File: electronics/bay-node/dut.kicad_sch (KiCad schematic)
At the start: 24 parts, among them J5 AUX, Q2 2N7002, Q3 2N7002, U10 INA226AIDGSR, U9 TPS2553DBVR

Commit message: Hub 37 and node 38 part types: more values merged
From the JLC cost session's list (it does the analysis, this session
edits the boards).  No footprint or track moves; both boards regenerated
on their Freerouting sessions (node 996/386, hub 1241/593 segments/vias),
ERC 0, DRC 0 errors (the hub's known C8 silkscreen warning), parity 0.

- Hub: the IMON filters and the CAN split caps on the dVdT caps' 22 nF
  (IMON RC 22 µs; the split cap only filters common mode): 38 -> 37 types,
  -$17.05 of feeders against the quote, order ≈ $212.77.
- Node: buck EN 100k/10k (same 13.5 V / 10.8 V), PC_DET 10k/18k (3.2 V),
  I²C pull-ups 5.1k, AUX VREF 33 Ω: 42 -> 38 types, estimate ≈ $322.77.

Docs: electronics.md (the hub's types per block, the node's estimate),
can.md, firmware pin tables.

Co-Authored-By: Claude Opus 5.5 <noreply@anthropic.com>
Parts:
- R21, R22: value 4.7k -> 5.1k; LCSC C23162 -> C23186; MPN 0603WAF4701T5E -> 0603WAF5101T5E
- R23: value 10 -> 33; LCSC C22859 -> C23140; MPN 0603WAF100JT5E -> 0603WAF330JT5E
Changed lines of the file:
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@@
 			)
 		)
-		(property "Value" "4.7k"
+		(property "Value" "5.1k"
 			(at 258.116 53.34 0)
 			(effects
@@
 			)
 		)
-		(property "Description" "Resistor 4.7k 0603"
+		(property "Description" "Resistor 5.1k 0603"
 			(at 254 52.07 0)
 			(effects
@@
 			)
 		)
-		(property "LCSC" "C23162"
+		(property "LCSC" "C23186"
 			(at 254 52.07 0)
 			(effects
@@
 			)
 		)
-		(property "MPN" "0603WAF4701T5E"
+		(property "MPN" "0603WAF5101T5E"
 			(at 254 52.07 0)
 			(effects
@@
 			)
 		)
-		(property "Value" "4.7k"
+		(property "Value" "5.1k"
 			(at 278.436 53.34 0)
 			(effects
@@
 			)
 		)
-		(property "Description" "Resistor 4.7k 0603"
+		(property "Description" "Resistor 5.1k 0603"
 			(at 274.32 52.07 0)
 			(effects
@@
 			)
 		)
-		(property "LCSC" "C23162"
+		(property "LCSC" "C23186"
 			(at 274.32 52.07 0)
 			(effects
@@
 			)
 		)
-		(property "MPN" "0603WAF4701T5E"
+		(property "MPN" "0603WAF5101T5E"
 			(at 274.32 52.07 0)
 			(effects
@@
 			)
 		)
-		(property "Value" "10"
+		(property "Value" "33"
 			(at 229.87 139.776 90)
 			(effects
@@
 			)
 		)
-		(property "Description" "Resistor 10 0603"
+		(property "Description" "Resistor 33 0603"
 			(at 229.87 137.16 0)
 			(effects
@@
 			)
 		)
-		(property "LCSC" "C22859"
+		(property "LCSC" "C23140"
 			(at 229.87 137.16 0)
 			(effects
@@
 			)
 		)
-		(property "MPN" "0603WAF100JT5E"
+		(property "MPN" "0603WAF330JT5E"
 			(at 229.87 137.16 0)
 			(effects
@@
 		)
 	)
-	(text_box "TPS2553: ILIM 18k → 1.34–1.52 A.  EN is pulled up: DUT_5V is on\n  even with no firmware; ~FAULT flags current limit / over-temperature.\nINA226 (I2C 0x40) runs from +3V3: it measures the drop across\n  R19 (50 mΩ → 1.64 A full scale, Kelvin sense pads); Vbus on Vin-: DUT_5V at the shunt.\nAUX: TX/RX through 1k, VREF = +3V3 through 10 Ω (level hint),\n  RESET/BOOT open-drain (2N7002, 100k gate pull-downs)."
+	(text_box "TPS2553: ILIM 18k → 1.34–1.52 A.  EN is pulled up: DUT_5V is on\n  even with no firmware; ~FAULT flags current limit / over-temperature.\nINA226 (I2C 0x40) runs from +3V3: it measures the drop across\n  R19 (50 mΩ → 1.64 A full scale, Kelvin sense pads); Vbus on Vin-: DUT_5V at the shunt.\nAUX: TX/RX through 1k, VREF = +3V3 through 33 Ω (level hint),\n  RESET/BOOT open-drain (2N7002, 100k gate pull-downs)."
 		(exclude_from_sim no)
 		(at 15.24 132.08 0)

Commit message: Node U9 TPS2553D; hub input FETs stay 40 V
Three checks from a BOM review:

- Node U9: the TPS2553DDBVR (C521201, $0.19 against $0.54) instead of
  the TPS2553DBVR.  Same SOT-23-6 pinout (IN GND EN FAULT ILIM OUT, EN
  active high), the same I_LIM equations (18k: 1.34-1.52 A), 85 mΩ,
  constant current then thermal cycling, plus reverse-voltage
  protection.  JLC's EasyEDA footprint for it is turned 90° from the old
  part's: CPL correction 270° (fitted pad by pad, as the TPS2553-1's).
  There is no latch-off D part: the DATA x4 keeps the TPS2553DBVR-1.
- Hub Q1/Q2 stay IRF7842 (40 V).  The AP33772S drives the gate at most
  4 V above VCC, so R_DS(on) at 4.5 V decides (5.9 mΩ max); Diodes' EVB
  uses 30 V parts; 60 V SO-8 parts in stock are ≥ 28 mΩ there.  Q1 sees
  > 40 V only with the switch open, VRACK discharged and a > 4 A surge
  into the SMAJ30A; the IRF7842 is avalanche-rated (50 mJ, 14 A).
- Node C11 stays 0805: a 1206 overlaps U2 and its neighbours.

The node regenerated on its Freerouting session (996 segments, 386
vias): ERC 0, DRC 0, parity 0.  Estimate ≈ $318.85.

Co-Authored-By: Claude Opus 5.5 <noreply@anthropic.com>
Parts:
- U9: value TPS2553DBVR -> TPS2553DDBVR; Alternative (none) -> TPS2553DBVR (C55266, the original, same pinout and I_LIM eq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; LCSC C55266 -> C521201; MPN TPS2553DBVR -> TPS2553DDBVR
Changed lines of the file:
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@@
 			)
 		)
-		(property "Value" "TPS2553DBVR"
-			(at 97.215 68.58 0)
+		(property "Value" "TPS2553DDBVR"
+			(at 97.74 68.58 0)
 			(effects
 				(font
@@
 			)
 		)
-		(property "Datasheet" "https://www.ti.com/lit/ds/symlink/tps2553.pdf"
+		(property "Datasheet" "https://www.ti.com/lit/ds/symlink/tps2553d.pdf"
 			(at 101.6 76.2 0)
 			(effects
@@
 			)
 		)
-		(property "MPN" "TPS2553DBVR"
+		(property "MPN" "TPS2553DDBVR"
 			(at 101.6 76.2 0)
 			(effects
@@
 			)
 		)
-		(property "LCSC" "C55266"
+		(property "LCSC" "C521201"
 			(at 101.6 76.2 0)
 			(effects
+				(font
+					(size 1.27 1.27)
+				)
+				(hide yes)
+			)
+		)
+		(property "Alternative" "TPS2553DBVR (C55266, the original, same pinout and I_LIM equations)"
+			(at 101.6 76.2 0)
+			(effects

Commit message: PCBA review: hub and node fixes before the order
On main's CH224A hub and the bay node v0.5.

Power hub:
- CPL: the side LEDs (C598310, C4555382) +0.825 mm, their polarity
  proven from JLC's own footprints (and C495809 at 270 deg in the table,
  for the IRF7842 the AP33772S hub had).
- Rows: SHDN pull-downs 10k, so rows stay off without firmware (100k
  gave 1 V at the pin's 10 uA); a B5819W at each row output for the
  cable's kick; the red FAULT LEDs fed from their ROW_EN, so a row that
  is simply off shows no fault.
- In2's VRACK band 8 mm wide; the console's USB pair hand-routed on
  F.Cu over In1 (U5's channels in the pair's order), EN's capacitor at
  the module's pin; reliefs on both pads of C2, C10, R3, C11-C14; notes
  corrected, the outputs sheet on A2.
- The PESD2CAN kept and documented (no stocked CAN TVS stays off at
  29.4 V and clamps under +40 V).

Bay node:
- SW3 placed on its pegs (-0.55 mm, Shouhan's land pattern); 2.2k I2C
  pull-ups; POS_IN 470k; AUX_VREF 1k; 100k on SVC; U9's input on a +5V
  island with three vias, C20 at its pins; C12 relieved; the camera note
  and the catalog's MPN text corrected.

Both re-routed: ERC 0, DRC 0 (the known C8 silkscreen warning), parity
0; CPL audit against JLC's footprints: every part agrees but SW3's pads
(0.13 mm, on purpose).  Bring-up measurements in assembly.md, the
resolution in pcba-review.md.

Co-Authored-By: Claude Opus 5.5 <noreply@anthropic.com>
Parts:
- R19: MPN HoLR1206-1W-50mR-1% -> HoLR1206-1W-50mR-1%-75ppm
- R21, R22: value 5.1k -> 2.2k; LCSC C23186 -> C4190; MPN 0603WAF5101T5E -> 0603WAF2201T5E
- R23: value 33 -> 1k; LCSC C23140 -> C21190; MPN 0603WAF330JT5E -> 0603WAF1001T5E
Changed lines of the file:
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@@
 			)
 		)
-		(property "MPN" "HoLR1206-1W-50mR-1%"
+		(property "MPN" "HoLR1206-1W-50mR-1%-75ppm"
 			(at 157.48 85.09 0)
 			(effects
@@
 			)
 		)
-		(property "Value" "5.1k"
+		(property "Value" "2.2k"
 			(at 258.116 53.34 0)
 			(effects
@@
 			)
 		)
-		(property "Description" "Resistor 5.1k 0603"
+		(property "Description" "Resistor 2.2k 0603"
 			(at 254 52.07 0)
 			(effects
@@
 			)
 		)
-		(property "LCSC" "C23186"
+		(property "LCSC" "C4190"
 			(at 254 52.07 0)
 			(effects
@@
 			)
 		)
-		(property "MPN" "0603WAF5101T5E"
+		(property "MPN" "0603WAF2201T5E"
 			(at 254 52.07 0)
 			(effects
@@
 			)
 		)
-		(property "Value" "5.1k"
+		(property "Value" "2.2k"
 			(at 278.436 53.34 0)
 			(effects
@@
 			)
 		)
-		(property "Description" "Resistor 5.1k 0603"
+		(property "Description" "Resistor 2.2k 0603"
 			(at 274.32 52.07 0)
 			(effects
@@
 			)
 		)
-		(property "LCSC" "C23186"
+		(property "LCSC" "C4190"
 			(at 274.32 52.07 0)
 			(effects
@@
 			)
 		)
-		(property "MPN" "0603WAF5101T5E"
+		(property "MPN" "0603WAF2201T5E"
 			(at 274.32 52.07 0)
 			(effects
@@
 			)
 		)
-		(property "Value" "33"
+		(property "Value" "1k"
 			(at 229.87 139.776 90)
 			(effects
@@
 			)
 		)
-		(property "Description" "Resistor 33 0603"
+		(property "Description" "Resistor 1k 0603"
 			(at 229.87 137.16 0)
 			(effects
@@
 			)
 		)
-		(property "LCSC" "C23140"
+		(property "LCSC" "C21190"
 			(at 229.87 137.16 0)
 			(effects
@@
 			)
 		)
-		(property "MPN" "0603WAF330JT5E"
+		(property "MPN" "0603WAF1001T5E"
 			(at 229.87 137.16 0)
 			(effects

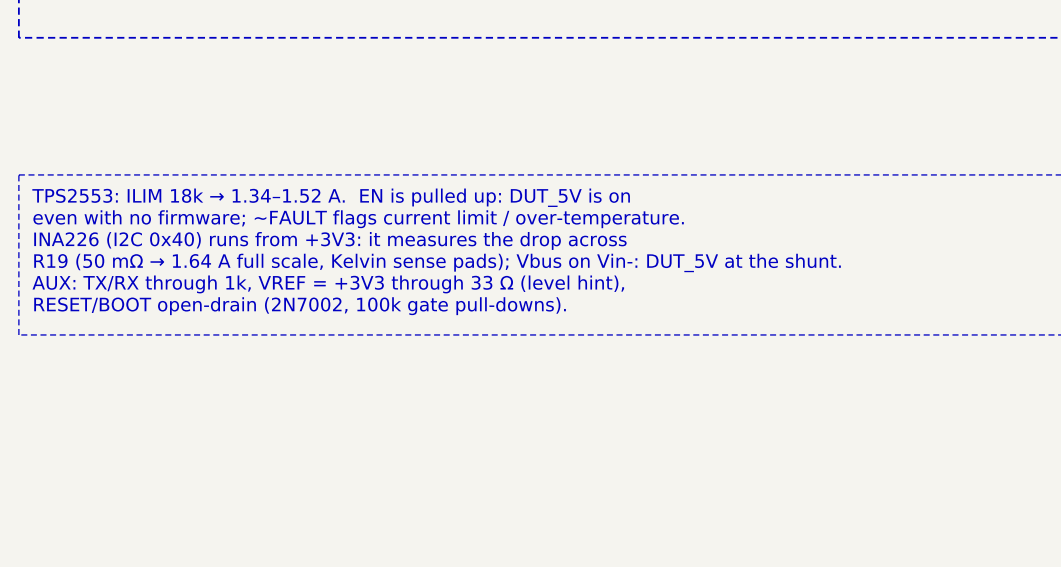
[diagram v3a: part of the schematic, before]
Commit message: Bay node: AP2114H for the 3.3 V, camera ESD clamped to +3V3
The schematic counter-review's fixes, approved by the user.

- U2: AP2114H-3.3TRG1 (C150716, catalog ldo_1a) instead of the AMS1117-3.3.
  It is specified stable with ceramics (C11, C12); the AMS1117 guarantees it
  only with 22 uF tantalum.  Same SOT-223 "H" pinout (1 GND, 2 and tab VOUT,
  3 VIN), footprint and copper: only the part's properties change.
- U12, U13 (USBLC6 on the camera lead): pin 5 on +3V3 instead of CAM_5V.
  With CAM_5V off (the PTC tripped), the SPI lines would feed the pod through
  the upper diodes, and CAM_5V's clamp sits above the ESP32's 3.6 V.  A
  minimal patch of the routing, no re-route: the CAM_5V stub that only
  reached the two pins goes (10 segments); U12.5 gets a +3V3 feed to a via in
  In2's +3V3 area; U13.5, with no room for its own, joins U12.5 along the
  stub's old east path at 0.25 mm.  The straightening pass ran on +3V3 and
  CAM_5V.
- Stale notes: AUX_VREF goes through R23's 1k, not 33 ohms; the next node's
  pull-down is R29's 470k, not 100k.
- pcbgen.fanout_pads takes `only` (REF.PAD), to fan out a few pads of a
  routed board.

ERC 0, DRC 0, unconnected 0, parity 0, every 3D model found.  The renders,
Gerbers and viewer model are regenerated (the unchanged iso render kept).
The schematic, the BOM and the docs (the node table, the CPL fix table, the
bring-up check, PCBA review N9) follow.  The hub and bom/ are untouched.

Co-Authored-By: Claude Opus 5.5 <noreply@anthropic.com>
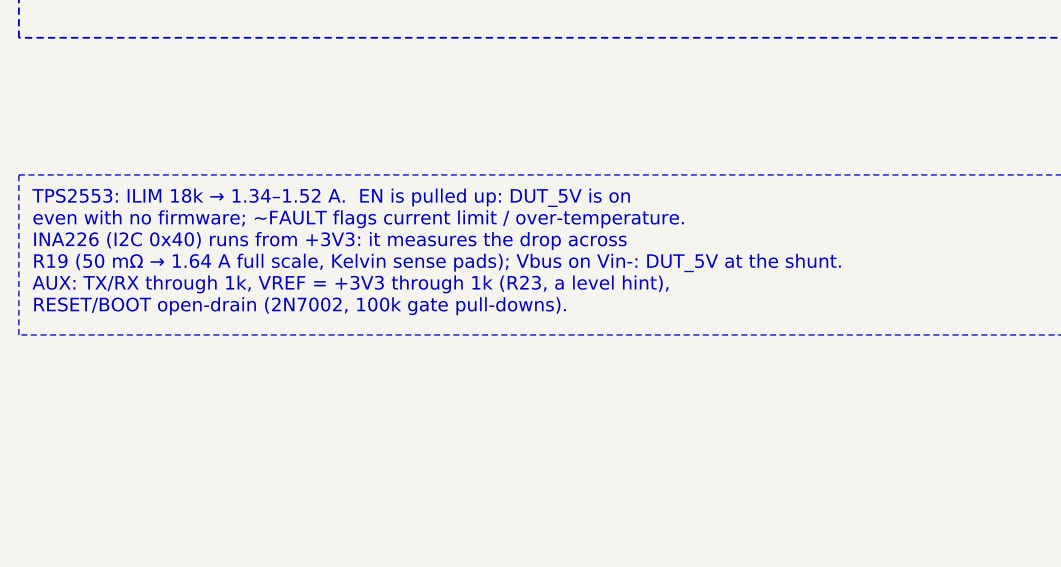
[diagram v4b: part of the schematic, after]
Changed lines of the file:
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@@
 		)
 	)
-	(text_box "TPS2553: ILIM 18k → 1.34–1.52 A.  EN is pulled up: DUT_5V is on\n  even with no firmware; ~FAULT flags current limit / over-temperature.\nINA226 (I2C 0x40) runs from +3V3: it measures the drop across\n  R19 (50 mΩ → 1.64 A full scale, Kelvin sense pads); Vbus on Vin-: DUT_5V at the shunt.\nAUX: TX/RX through 1k, VREF = +3V3 through 33 Ω (level hint),\n  RESET/BOOT open-drain (2N7002, 100k gate pull-downs)."
+	(text_box "TPS2553: ILIM 18k → 1.34–1.52 A.  EN is pulled up: DUT_5V is on\n  even with no firmware; ~FAULT flags current limit / over-temperature.\nINA226 (I2C 0x40) runs from +3V3: it measures the drop across\n  R19 (50 mΩ → 1.64 A full scale, Kelvin sense pads); Vbus on Vin-: DUT_5V at the shunt.\nAUX: TX/RX through 1k, VREF = +3V3 through 1k (R23, a level hint),\n  RESET/BOOT open-drain (2N7002, 100k gate pull-downs)."
 		(exclude_from_sim no)
 		(at 15.24 132.08 0)

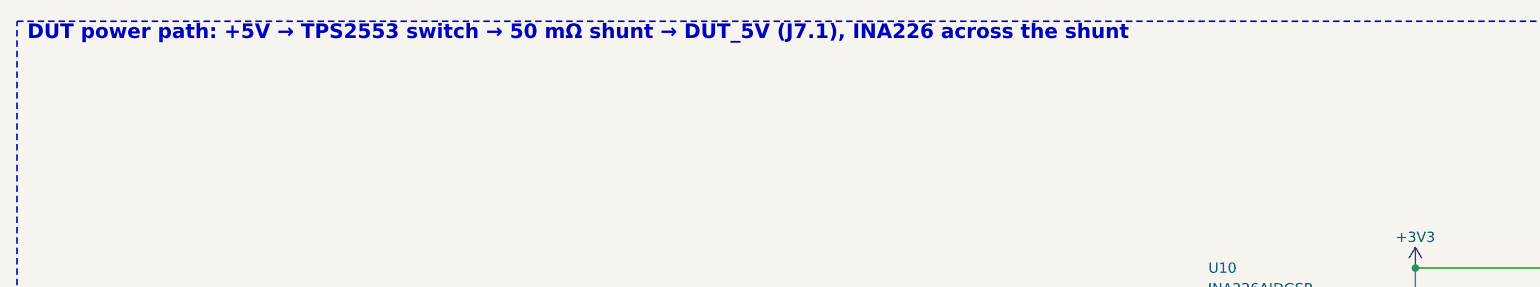
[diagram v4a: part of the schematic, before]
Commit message: Datasheet audit F1-F6: the pod's AP2114H, STB 5.1k, PC_DET hysteresis, the camera ESD's 100 nF, the eFuse step
The user approved the audit's fixes for the node, the hub and the pod
("Go pour 1"); docs/datasheet-audit.md marks F1-F6 applied.

* F1, camera pod: U1 AMS1117-3.3 -> AP2114H-3.3TRG1 (C150716, catalog
  ldo_1a, the node's U2).
  - The AMS1117 is specified stable only with 22 uF tantalum; the
    AP2114H is stable with the ceramic C2.
  - Same SOT-223 pinout, copper (the +3V3 pour and island round the
    tab stay) and 180 deg CPL correction.
  - One more extended type on the pod's Economic order: +$3.09 and
    $0.05 of parts (JLC_SINCE_QUOTE).
* F2, power hub: R214 (TJA1462 STB pull-down) 10k -> 5.1k (C23186,
  already on the board). With IO9 floating, STB's internal pull-up
  (20 kOhm minimum) left it at up to 1.10 V, over VIL 0.99 V.
* F3, bay node: R42 150k from MUX_SEL back to PC_DET, beside U7 (C22807,
  on the board since S1).
  - The laptop's VBUS rises at ~50 us/V through R11/R12, where the
    LVC1G32 wants <= 10 ns/V and warns of oscillation.
  - This gives ~0.14 V of hysteresis.
* F4, bay node: C28 100 nF (C14663) on U12/U13's VBUS pins (+3V3), above
  U12 by its pin 5. Between the two ICs their courtyards leave no room.
* F5, node and hub: firmware.md's first-flash procedure gains the
  irreversible DIS_USB_OTG_DOWNLOAD_MODE eFuse step. In USB-OTG
  download boot the ROM drives IO40 high: the node's DUT_FLT_N, the
  hub's PD_SCL. Nothing is burnt.
* F6, notes, hub:
  - the IMON filter is 0.9 ms, not 47 us: the pin is a current source;
  - the buck stops at ~3.8 V (internal UVLO);
  - SHDN turns on at >= 1 V;
  - the soft start stays under the limit only typically;
  - the CH224A note follows CH224 V2.1: the source PDOs are listed for
    both parts and readable under 100 W, which is still to check with
    ours (review R3); single-byte transfers; no "same die".
* F6, notes, node: TPS2553D; the LDO's 1.94 V x 0.4 A ~ 0.8 W; L1's
  7.5 A guarante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
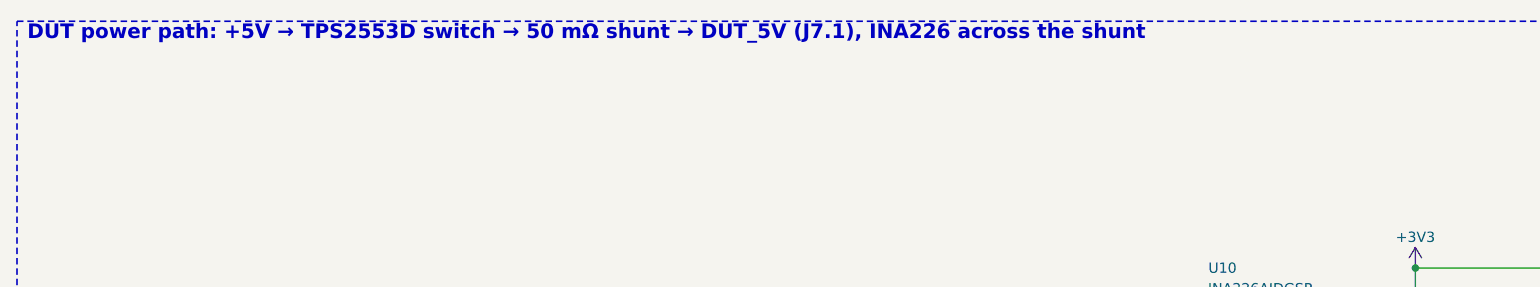
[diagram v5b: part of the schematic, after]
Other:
- note added: "DUT power path: +5V → TPS2553D switch → 50 mΩ shunt → DUT_5V (J7.1), INA226 across the shunt"
- note removed: "DUT power path: +5V → TPS2553 switch → 50 mΩ shunt → DUT_5V (J7.1), INA226 across the shunt"
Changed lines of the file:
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@@
 		(comment 1 "ESP32-S3 USB/IP host for one bay of the hw-testing-rack shelf")
 		(comment 2 "Generated from electronics/bay-node/design.py — edit the Python, then regenerate")
-		(comment 3 "Row bus 20–28 V + CAN + POS in/out · 5 V/1.4 A switched DUT port · USB 2.0 muxes · INA226 · AUX")
+		(comment 3 "Row bus 20–28 V + CAN + POS in/out · 5 V/1.4 A switched DUT power on the DATA lead · USB 2.0 muxes · INA226 · AUX")
 	)
 	(symbol
@@
 		)
 	)
-	(text "DUT power path: +5V → TPS2553 switch → 50 mΩ shunt → DUT_5V (J7.1), INA226 across the shunt"
+	(text "DUT power path: +5V → TPS2553D switch → 50 mΩ shunt → DUT_5V (J7.1), INA226 across the shunt"
 		(exclude_from_sim no)
 		(at 16.51 33.02 0)
